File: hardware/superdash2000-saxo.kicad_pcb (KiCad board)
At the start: 2 copper layers, 4 parts, among them U1 L7805

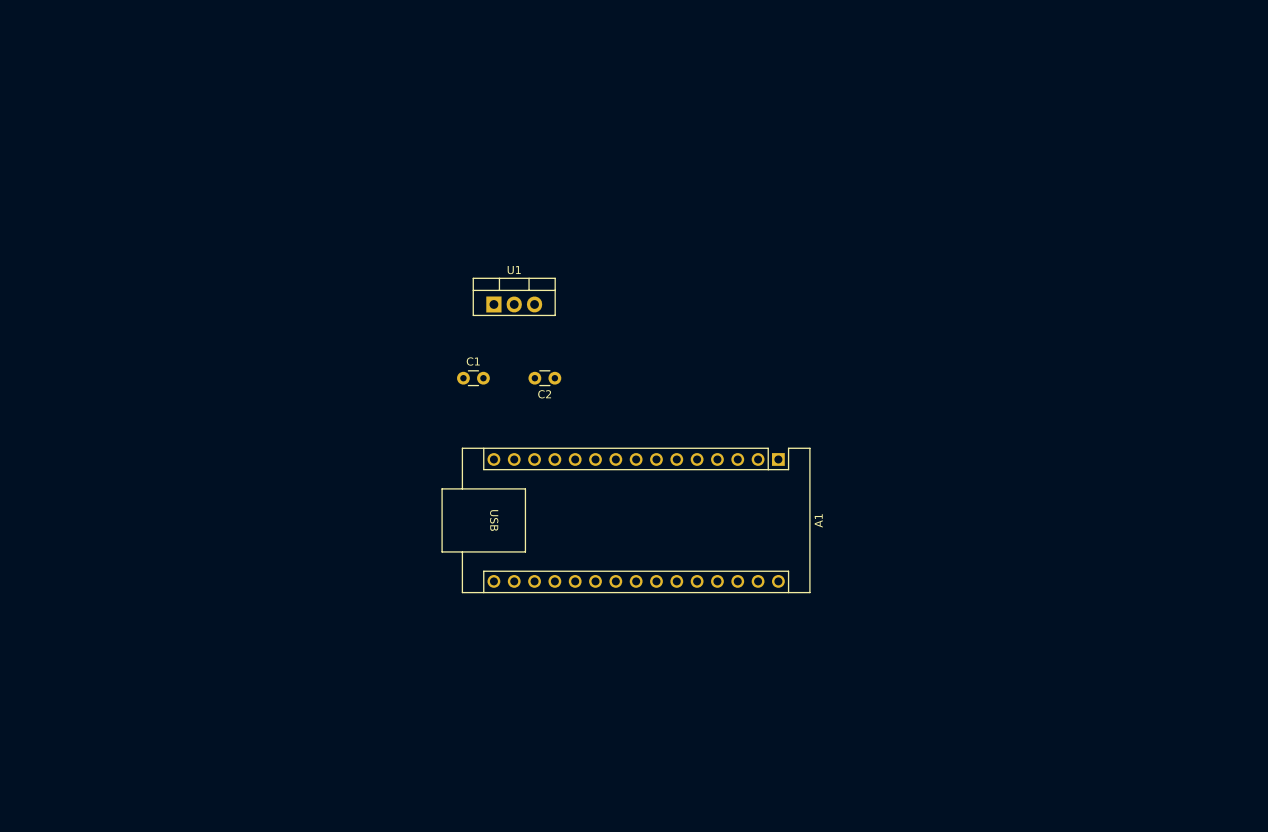
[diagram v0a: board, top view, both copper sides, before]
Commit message: hardware: Update footprints
Signed-off-by: Thomas Antonini <antonini.thomas@gmail.com>
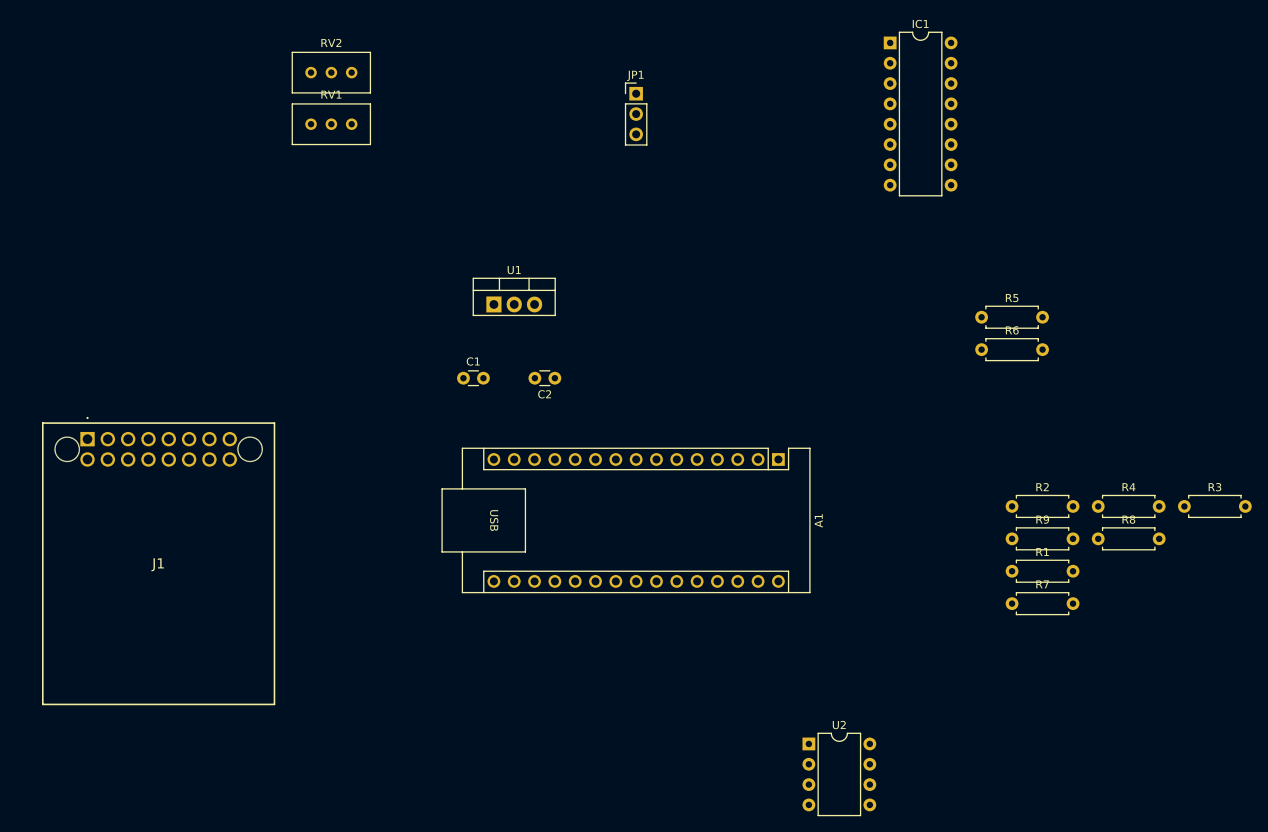
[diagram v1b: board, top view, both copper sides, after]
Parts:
- added IC1: MAX4617CPE+, Package_DIP:DIP-16_W7.62mm, F.Cu at (138.4, 33.0)
- added J1: Molex 34691-0161, Molex_34691-0161:Molex 34691-0161, F.Cu at (38.1, 82.5)
- added JP1: Jumper_3_Bridged12, Connector_PinHeader_2.54mm:PinHeader_1x03_P2.54mm_Vertical, F.Cu at (106.7, 39.4)
- added R1: R, Resistor_THT:R_Axial_DIN0207_L6.3mm_D2.5mm_P7.62mm_Horizontal, F.Cu at (153.7, 99.1)
- added R2: R, Resistor_THT:R_Axial_DIN0207_L6.3mm_D2.5mm_P7.62mm_Horizontal, F.Cu at (153.7, 91.0)
- added R3: R, Resistor_THT:R_Axial_DIN0207_L6.3mm_D2.5mm_P7.62mm_Horizontal, F.Cu at (175.2, 91.0)
- added R4: R, Resistor_THT:R_Axial_DIN0207_L6.3mm_D2.5mm_P7.62mm_Horizontal, F.Cu at (164.4, 91.0)
- added R5: R, Resistor_THT:R_Axial_DIN0207_L6.3mm_D2.5mm_P7.62mm_Horizontal, F.Cu at (149.9, 67.3)
- added R6: R, Resistor_THT:R_Axial_DIN0207_L6.3mm_D2.5mm_P7.62mm_Horizontal, F.Cu at (149.9, 71.4)
- added R7: R, Resistor_THT:R_Axial_DIN0207_L6.3mm_D2.5mm_P7.62mm_Horizontal, F.Cu at (153.7, 103.1)
- added R8: R, Resistor_THT:R_Axial_DIN0207_L6.3mm_D2.5mm_P7.62mm_Horizontal, F.Cu at (164.4, 95.0)
- added R9: R, Resistor_THT:R_Axial_DIN0207_L6.3mm_D2.5mm_P7.62mm_Horizontal, F.Cu at (153.7, 95.0)
- added RV1: R_Potentiometer, Potentiometer_THT:Potentiometer_Bourns_3296W_Vertical, F.Cu at (71.1, 43.2)
- added RV2: R_Potentiometer, Potentiometer_THT:Potentiometer_Bourns_3296W_Vertical, F.Cu at (71.1, 36.7)
- added U2: TLV2372, Package_DIP:DIP-8_W7.62mm, F.Cu at (128.3, 120.7)
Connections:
- net /5V renamed +5V
- net VCC renamed Net-(C1-Pad1)
- A1 pad 10: unconnected-(A1-Pad10) -> /D7
- A1 pad 19: unconnected-(A1-Pad19) -> /A0
- A1 pad 23: unconnected-(A1-Pad23) -> /LCD_SDA
- A1 pad 24: unconnected-(A1-Pad24) -> /LCD_SCL
- A1 pad 30: unconnected-(A1-Pad30) -> /VIN
- A1 pad 5: unconnected-(A1-Pad5) -> /D2
- A1 pad 6: unconnected-(A1-Pad6) -> /D3
- A1 pad 7: unconnected-(A1-Pad7) -> /D4
- A1 pad 8: unconnected-(A1-Pad8) -> /D5
- A1 pad 9: unconnected-(A1-Pad9) -> /D6

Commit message: hardware: Place components on pcb
Signed-off-by: Thomas Antonini <antonini.thomas@gmail.com>
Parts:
- added C3: C, Capacitor_THT:C_Disc_D5.0mm_W2.5mm_P2.50mm, F.Cu at (72.4, 64.8)
- added F1: 37201000431, Littlefuse_37201000431:37201000431, F.Cu at (39.4, 61.0)
- C1, C2: footprint Capacitor_THT:C_Disc_D3.0mm_W1.6mm_P2.50mm -> Capacitor_THT:C_Disc_D5.0mm_W2.5mm_P2.50mm
- moved R3 128.8 mm to (47.0, 102.8)
- moved R7 106.9 mm to (47.0, 110.5)
- moved R8 105.9 mm to (59.7, 110.4)
- moved R4 105.4 mm to (59.7, 102.8)
- moved IC1 94.8 mm to (83.8, 110.5), turned to 180 degrees
- moved R1 88.4 mm to (69.8, 71.1), turned to -90 degrees
- moved U2 87.1 mm to (41.9, 109.2), turned to 180 degrees
- moved R2 84.1 mm to (69.8, 84.0), turned to -90 degrees
- moved R9 82.0 mm to (77.5, 64.8)
- moved R5 70.4 mm to (91.4, 106.7)
- moved R6 70.4 mm to (91.4, 110.7)
- moved JP1 62.3 mm to (47.0, 57.1)
- moved RV1 41.0 mm to (82.2, 82.6)
- moved RV2 38.7 mm to (82.2, 73.8)
- moved C1 36.4 mm to (53.3, 57.1), turned to -90 degrees
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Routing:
- net GND: track 0.00 -> 15.4 mm
- added copper zone on B.Cu, net GND
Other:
- board outline added: 77.5 x 59.7 mm

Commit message: hardware: Update pcb
Signed-off-by: Thomas Antonini <antonini.thomas@gmail.com>
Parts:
- A1: footprint Module:Arduino_Nano -> Arduino_Nano_Every:Arduino_Nano_Every_WithMountingHoles
- moved R6 9.89 mm to (87.6, 101.6)
- moved U2 8.88 mm to (41.9, 100.3), turned to -90 degrees
- moved IC1 4.02 mm to (82.5, 106.7)
- moved R2 4.01 mm to (69.8, 80.0)
- moved R8 3.92 mm to (58.4, 106.7)
- moved R7 3.83 mm to (47.0, 106.7)
- moved R5 3.81 mm to (87.6, 106.7)
- moved A1 2.84 mm to (102.9, 95.2)
- moved C3 2.56 mm to (69.8, 64.8)
- moved R9 2.54 mm to (74.9, 64.8)
- moved C1 1.80 mm to (54.6, 58.4)
- moved R4 1.78 mm to (58.4, 101.6)
- moved R1 1.77 mm to (69.8, 69.3)
- moved C2 1.29 mm to (72.4, 58.4)
- moved U1 1.29 mm to (61.0, 60.6)
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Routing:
- net GND: track 15.4 -> 0.00 mm
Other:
- board size 77.5 x 59.7 mm -> 76.2 x 55.9 mm
